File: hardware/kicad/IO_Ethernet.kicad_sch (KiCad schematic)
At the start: 35 parts, among them U1 TPD4EUSB30, U2 TPD4EUSB30, U3 MagJack-A70-112-331N126, U5 74LVC1G07SE-7, U9 74LVC1G07SE-7

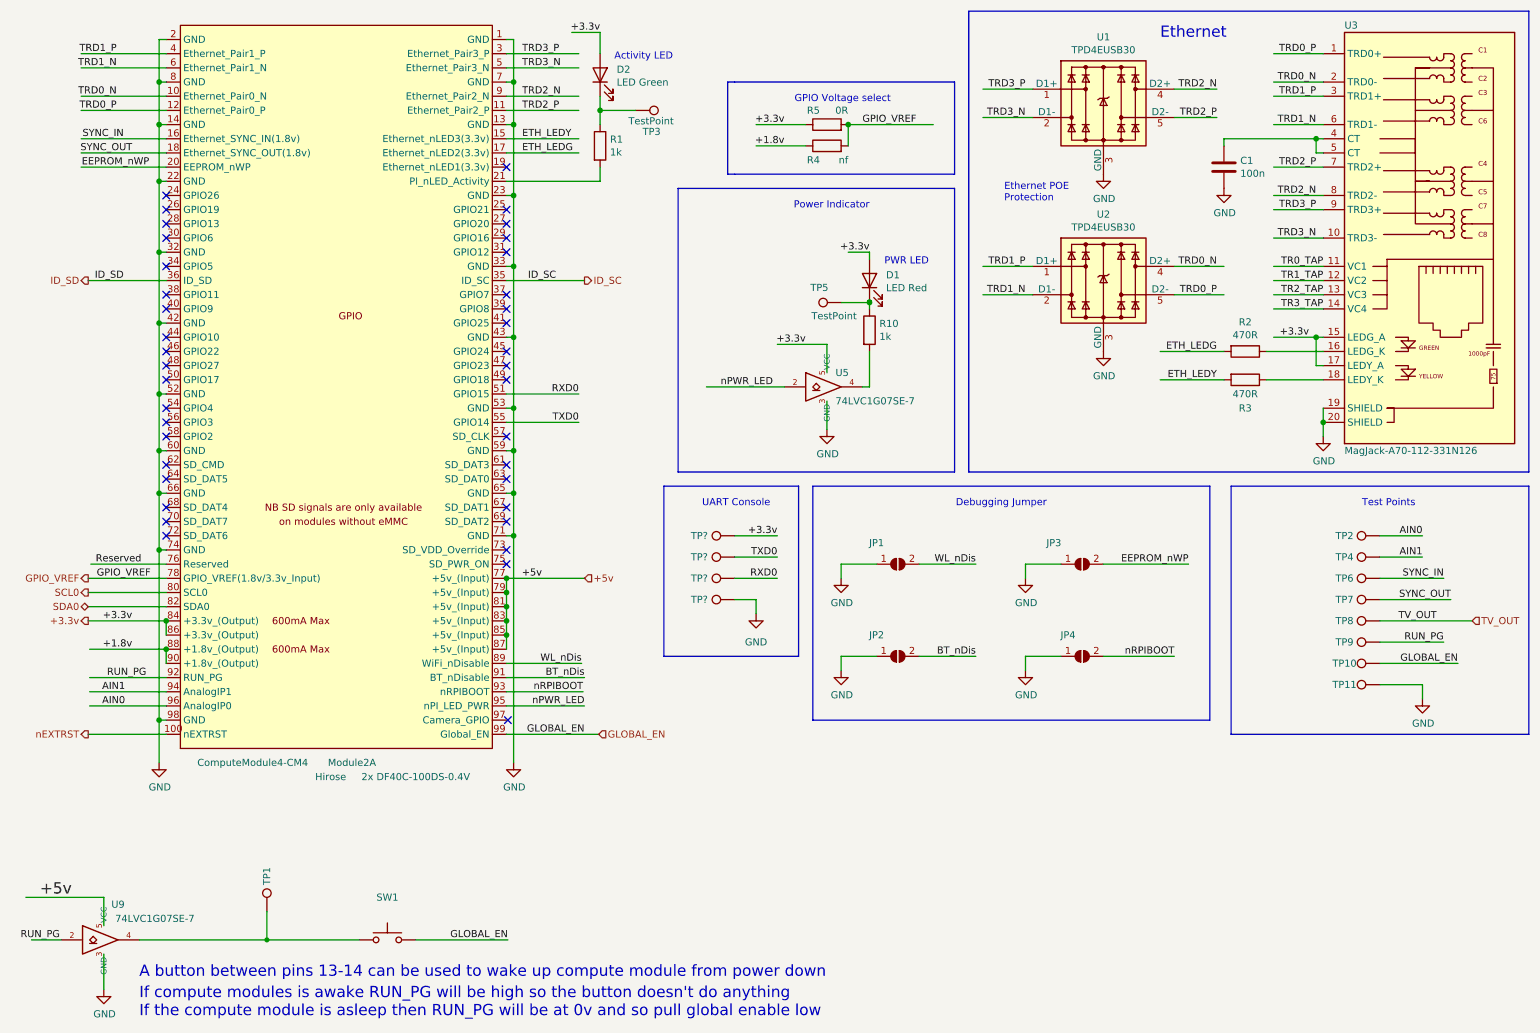
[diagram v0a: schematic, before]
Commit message: wire lorawan and swarm to cm4
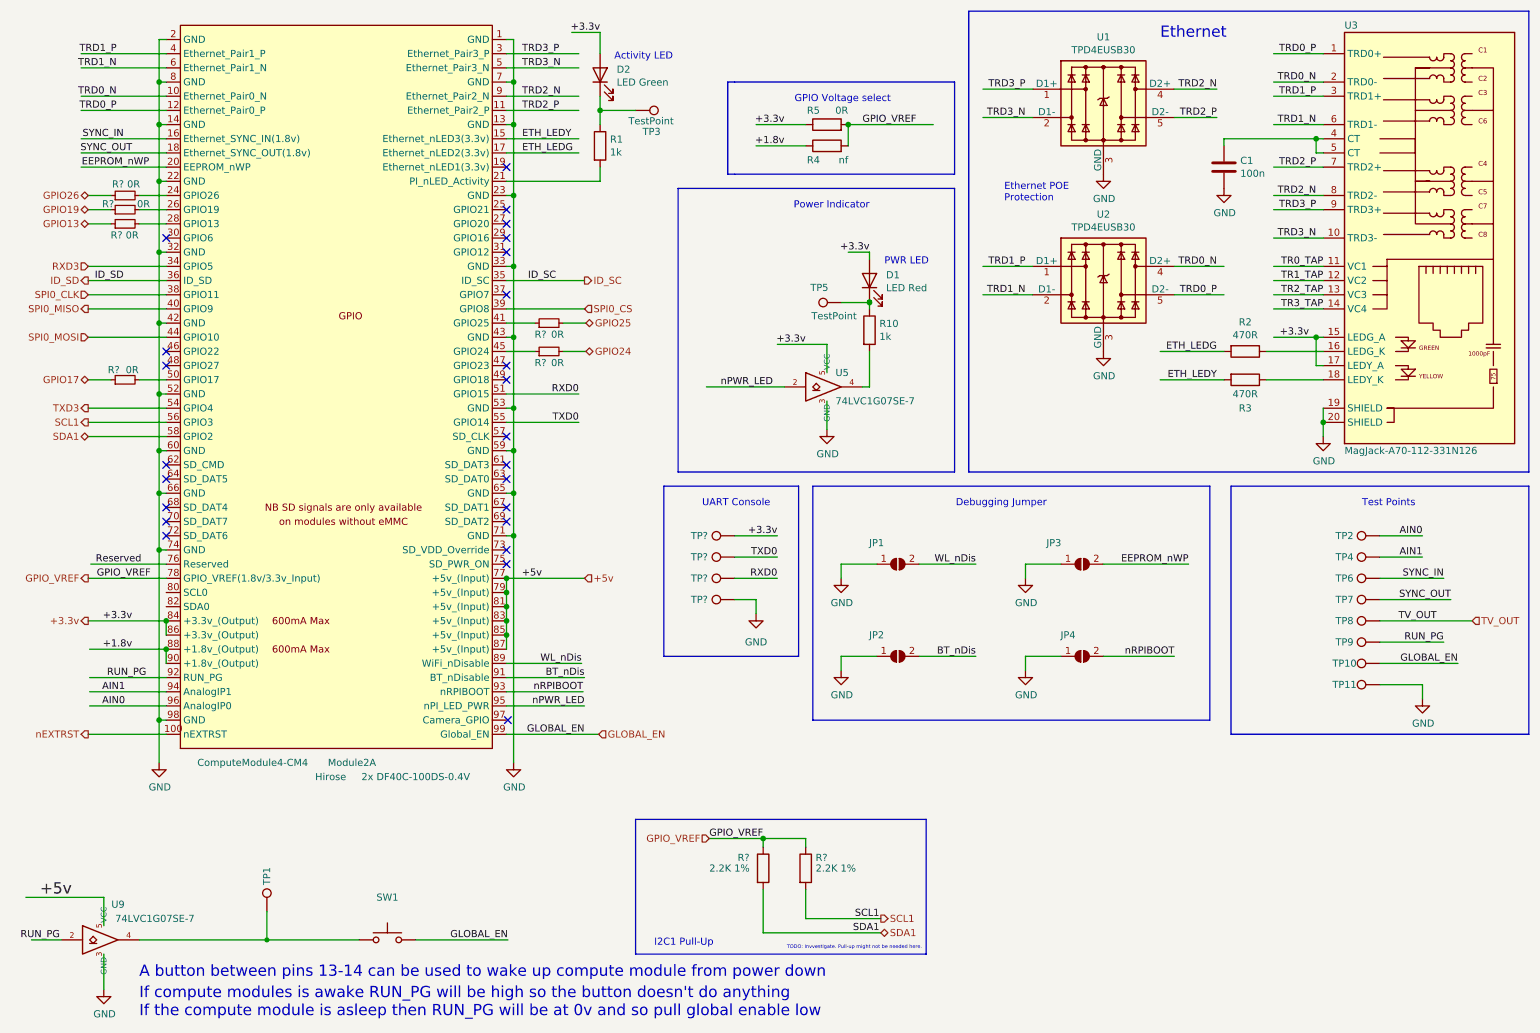
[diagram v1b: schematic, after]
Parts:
- added R? (x6): 0R, Resistor_SMD:R_0402_1005Metric, symbol Device:R_Small
- added R? (x2): 2.2K 1%, Resistor_SMD:R_0402_1005Metric, symbol Device:R
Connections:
- net GPIO_VREF: now also R?.1, R?.1
- net at Module2.24 (GPIO26): now also R?.2
- net at Module2.26 (GPIO19): now also R?.2
- net at Module2.28 (GPIO13): now also R?.2
- net RXD3: now reaches Module2.34 (GPIO5)
- net SPI0_CLK: now reaches Module2.38 (GPIO11)
- net SPI0_CS: now reaches Module2.39 (GPIO8)
- net SPI0_MISO: now reaches Module2.40 (GPIO9)
- net at Module2.41 (GPIO25): now also R?.1
- net SPI0_MOSI: now reaches Module2.44 (GPIO10)
- net at Module2.45 (GPIO24): now also R?.1
- net at Module2.50 (GPIO17): now also R?.2
- net TXD3: now reaches Module2.54 (GPIO4)
- net SCL1: now reaches Module2.56 (GPIO3)
- net SCL1: now also R?.2
- net SDA1: now reaches Module2.58 (GPIO2)
- net SDA1: now also R?.2
- net SCL0: no longer names the net of Module2.80 (SCL0)
- net SDA0: no longer names the net of Module2.82 (SDA0)
- new net GPIO13: R?.1
- new net GPIO17: R?.1
- new net GPIO19: R?.1
- new net GPIO24: R?.2
- new net GPIO25: R?.2
- new net GPIO26: R?.1
- no-connect marks 38 -> 24
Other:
- note added: "I2C1 Pull-Up"
- note added: "TODO: Invvestigate. Pull-up might not be needed here."

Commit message: initial pcb design
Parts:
- removed U1, U2: TPD4EUSB30, Package_SON:USON-10_2.5x1.0mm_P0.5mm, symbol Power_Protection:TPD4EUSB30
- added J3: BMS I2C, Connector_PinHeader_2.54mm:PinHeader_1x04_P2.54mm_Vertical, symbol Connector_Generic:Conn_01x04
- added U1, U2: (no value), symbol Teapot:TPD4EUSB30
- JP1: value ~ -> WL_DISABLE; footprint (none) -> Jumper:SolderJumper-2_P1.3mm_Open_RoundedPad1.0x1.5mm
- JP2: value ~ -> BT_DISABLE; footprint (none) -> Jumper:SolderJumper-2_P1.3mm_Open_RoundedPad1.0x1.5mm
- JP3: value ~ -> EEPROM_WP; footprint (none) -> Jumper:SolderJumper-2_P1.3mm_Open_RoundedPad1.0x1.5mm
- JP4: value ~ -> USB_BOOT; footprint (none) -> Jumper:SolderJumper-2_P1.3mm_Open_RoundedPad1.0x1.5mm
- SW1: value ~ -> Wake; footprint (none) -> Button_Switch_SMD:SW_SPST_TL3342
- TP1: footprint (none) -> TestPoint:TestPoint_Pad_D1.0mm
- TP10: value ~ -> GLOBAL_EN; footprint (none) -> TestPoint:TestPoint_Pad_D1.0mm
- TP11: value ~ -> GND; footprint (none) -> TestPoint:TestPoint_Pad_D1.0mm
- TP12: renamed from TP?; value ~ -> 3.3v; footprint (none) -> TestPoint:TestPoint_Pad_D1.0mm
- TP13: renamed from TP?; value ~ -> TXD0; footprint (none) -> TestPoint:TestPoint_Pad_D1.0mm
- TP14: renamed from TP?; value ~ -> RXD0; footprint (none) -> TestPoint:TestPoint_Pad_D1.0mm
- TP15: renamed from TP?; value ~ -> GND; footprint (none) -> TestPoint:TestPoint_Pad_D1.0mm
- TP2: value ~ -> AIN0; footprint (none) -> TestPoint:TestPoint_Pad_D1.0mm
- TP4: value ~ -> AIN1; footprint (none) -> TestPoint:TestPoint_Pad_D1.0mm
- TP6: value ~ -> SYNC_IN; footprint (none) -> TestPoint:TestPoint_Pad_D1.0mm
- TP7: value ~ -> SYNC_OUT; footprint (none) -> TestPoint:TestPoint_Pad_D1.0mm
- TP8: value ~ -> TV_OUT; footprint (none) -> TestPoint:TestPoint_Pad_D1.0mm
- TP9: value ~ -> RUN_PG; footprint (none) -> TestPoint:TestPoint_Pad_D1.0mm
- U3: footprint CM4IO:TRJG0926HENL -> Teapot:TRJG0926HENL
- gave numbers to parts that had none: 8
- renumbered Module2 to Module1
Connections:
- net +3.3v: now also J3.4 (Pin_4)
- net GND: now also J3.1 (Pin_1), U1.3 (GND), U1.8 (GND), U2.3 (GND), U2.8 (GND)
- net SCL1: now also J3.2 (Pin_2)
- net SDA1: now also J3.3 (Pin_3)
- net TRD0_N: now also U2.4 (D2+), U2.7
- net TRD0_P: now also U2.5 (D2-), U2.6
- net TRD1_N: now also U2.2 (D1-), U2.9
- net TRD1_P: now also U2.1 (D1+), U2.10
- net TRD2_N: now also U1.4 (D2+), U1.7
- net TRD2_P: now also U1.5 (D2-), U1.6
- net TRD3_N: now also U1.2 (D1-), U1.9
- net TRD3_P: now also U1.1 (D1+), U1.10
- no-connect marks 24 -> 26
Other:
- note added: "BMS I2C Connection"
- moved on the sheet: D1, JP1, JP2, JP3, JP4, R10, R23, R24, R4, R5, TP10, TP11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
